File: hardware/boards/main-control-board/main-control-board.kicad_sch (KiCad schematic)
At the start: 8 parts, among them J2 Conn_OLED, J3 Conn_extension, J4 Conn_extension_2

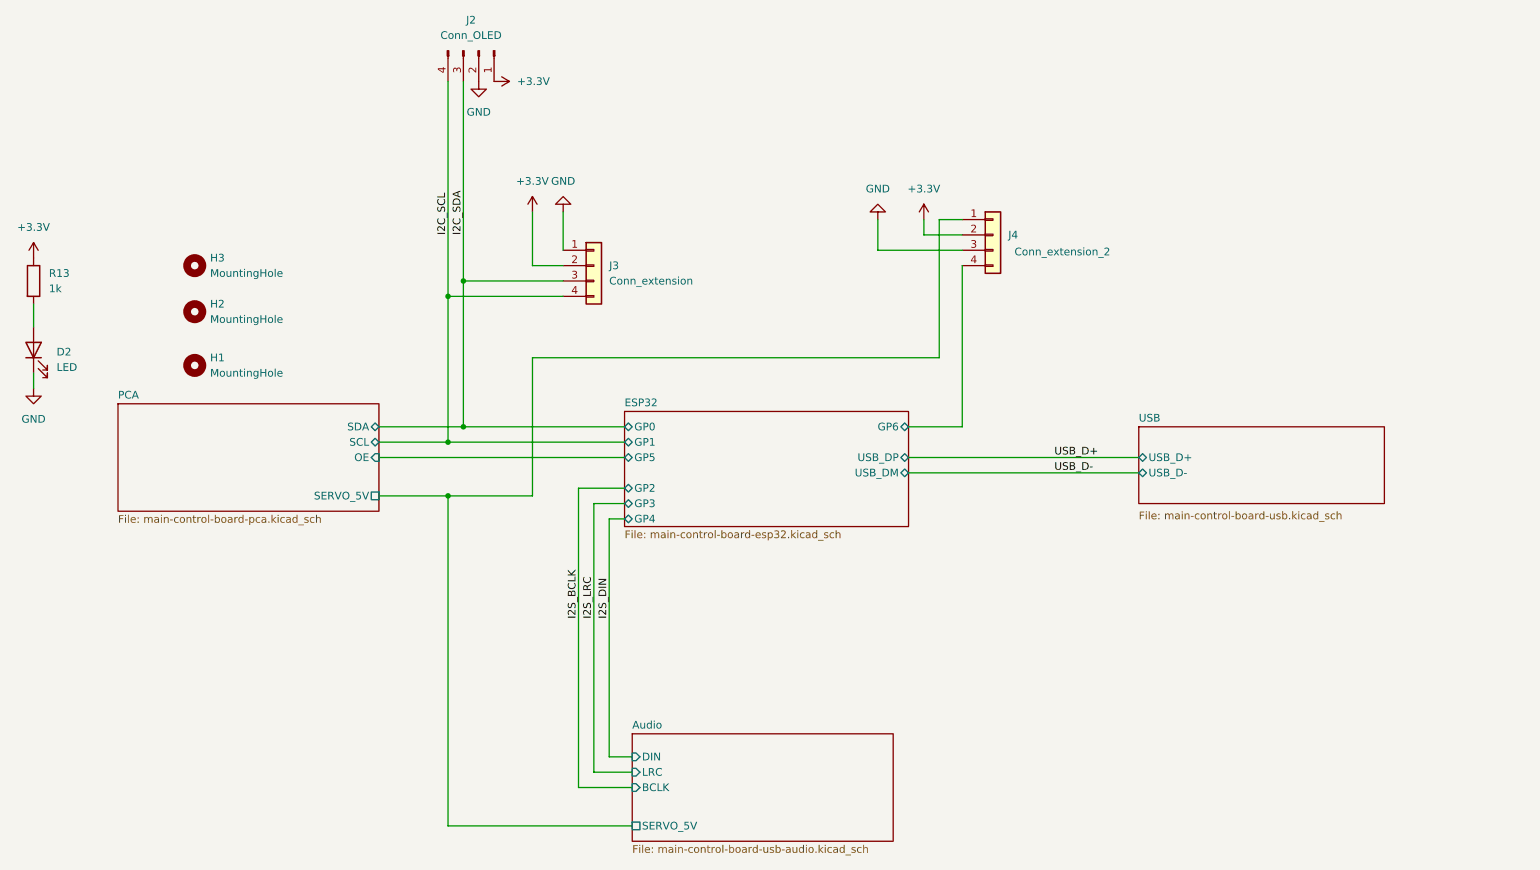
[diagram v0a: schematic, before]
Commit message: feat(pcb): main control board rev3 (#66, #62)
* add extension port

* update BOM

* update expected nets

* update README.md for main control board: clarify extension port details and specify strapping pins and UART connections

* update silkscreen layer for main control board: add knockout effect to VCC and voltage labels

* add ESP antenna keepout

* add 100nF to U4 dVdt

* add capacitor next to pin 28 of PCA

* update hardware documentation: clarify power distribution and GPIO pin usage on the main control board, including details on USB-C connections and extension headers

* update silkscreen text on main control board: change label from "GP9" to "BOOT" and modify "GP8" to "GP8*"

* docs(pcb): add main control board revision 3 preview image
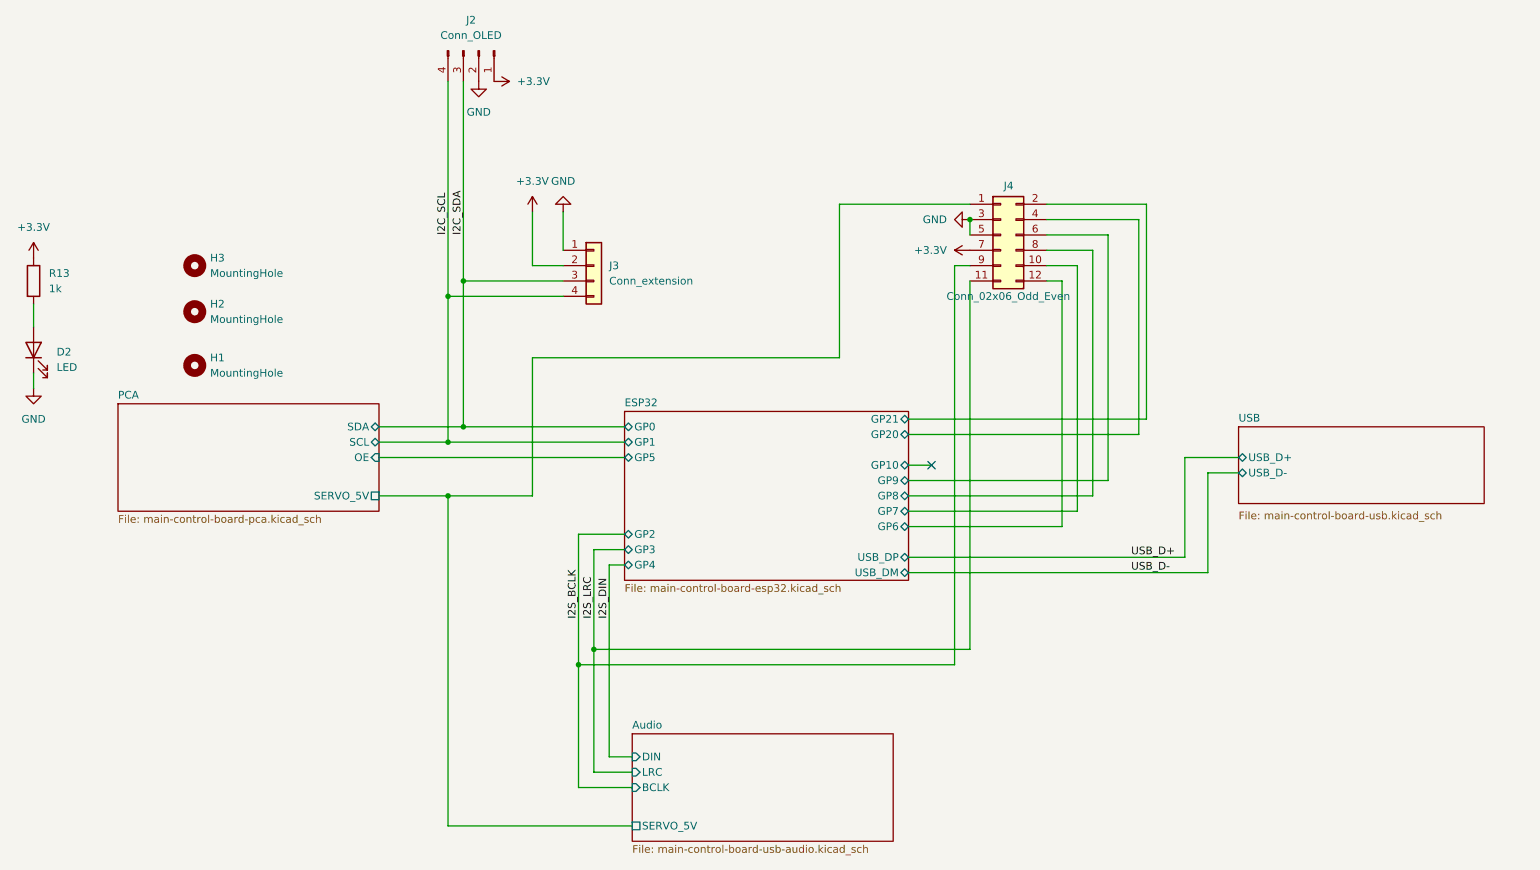
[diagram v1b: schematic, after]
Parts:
- J4: value Conn_extension_2 -> Conn_02x06_Odd_Even; footprint Connector_PinHeader_2.54mm:PinHeader_1x04_P2.54mm_Vertical -> Connector_PinHeader_2.54mm:PinHeader_2x06_P2.54mm_Vertical; symbol Connector_Generic:Conn_01x04 -> Connector_Generic:Conn_02x06_Odd_Even; FT Rotation Offset (none) -> 90; LCSC Part # (none) -> C541855; MPN (none) -> PM254V-12-12-H85; Manufacturer (none) -> XFCN; now in the parts list
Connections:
- net +3.3V: now also J4.7 (Pin_7); no longer J4.2 (Pin_2)
- net ESP32/GP6: now also J4.12 (Pin_12); no longer J4.4 (Pin_4)
- net GND: now also J4.5 (Pin_5)
- net I2S_BCLK: now also J4.9 (Pin_9)
- net I2S_LRC: now also J4.11 (Pin_11)
- new net ESP32/GP20: J4.4 (Pin_4)
- new net ESP32/GP21: J4.2 (Pin_2)
- new net ESP32/GP7: J4.10 (Pin_10)
- new net ESP32/GP8: J4.8 (Pin_8)
- new net ESP32/GP9: J4.6 (Pin_6)
- no-connect marks 0 -> 1
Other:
- sheet ESP32 ports: added GP10, GP20, GP21, GP7, GP8, GP9; removed none
